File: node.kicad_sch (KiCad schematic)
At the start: 13 parts, among them J3 STLINK/V2 Clone Header, U2 STM32L151RCTx

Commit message: feat: in progress rework
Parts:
- removed D18: Node Active LED, LED_SMD:LED_0603_1608Metric, symbol Device:LED
- removed J3: STLINK/V2 Clone Header, Connector_PinHeader_2.54mm:PinHeader_2x05_P2.54mm_Vertical, symbol Connector_Generic:Conn_02x05_Odd_Even
- removed R19: 5.1K, Resistor_SMD:R_0603_1608Metric, symbol Device:R
- added J3: USB-C, Connector_USB:USB_C_Receptacle_G-Switch_GT-USB-7010ASV, symbol Connector:USB_C_Receptacle_USB2.0_14P
- added J4: UART, symbol Connector_Generic:Conn_01x04
- added J8: TC2030, Connector:Tag-Connect_TC2030-IDC-FP_2x03_P1.27mm_Vertical, symbol Connector:Conn_ARM_SWD_TagConnect_TC2030
- added R16, R17: 5.1K, symbol Device:R
- added U3: USBLC6-2SC6, Package_TO_SOT_SMD:SOT-23-6, symbol Power_Protection:USBLC6-2SC6
- added Y1: 16MHz, symbol Device:Crystal_GND24
- R14: footprint Resistor_SMD:R_0603_1608Metric -> (none)
- U2: value STM32L151RCTx -> STM32L151RCT6
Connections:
- net +3V3: now also J4.1 (Pin_1), J8.1 (VCC)
- net CS_1: now also U2.33 (PB12); no longer U2.20 (PA4)
- net CS_10: now also U2.16 (PA2); no longer U2.4 (PC15)
- net CS_11: now also U2.15 (PA1); no longer U2.3 (PC14)
- net CS_12: now also U2.14 (PA0); no longer U2.2 (PC13)
- net CS_2: now also U2.30 (PB11); no longer U2.17 (PA3)
- net CS_3: now also U2.29 (PB10); no longer U2.16 (PA2)
- net CS_4: now also U2.27 (PB1); no longer U2.15 (PA1)
- net CS_5: now also U2.26 (PB0); no longer U2.14 (PA0)
- net CS_6: now also U2.25 (PC5); no longer U2.11 (PC3)
- net CS_7: now also U2.24 (PC4); no longer U2.10 (PC2)
- net CS_8: now also U2.20 (PA4); no longer U2.9 (PC1)
- net CS_9: now also U2.17 (PA3); no longer U2.8 (PC0)
- net GND: now also R14.2, J3.A1 (GND), J3.A12 (GND), J3.B1 (GND), J3.B12 (GND), J3.S1 (SHIELD), J4.4 (Pin_4), J8.5 (GND), R16.2, R17.2, U3.2 (GND), Y1.2, Y1.4; no longer R14.1
- net P_MISO: now also U2.35 (PB14); no longer U2.22 (PA6)
- net P_MOSI: now also U2.36 (PB15); no longer U2.23 (PA7)
- net P_SCLK: now also U2.34 (PB13); no longer U2.21 (PA5)
- net RESET: now also J8.3 (~{RESET})
- net R_CS: now also U2.11 (PC3); no longer U2.54 (PD2)
- net S_MISO: now also U2.22 (PA6); no longer U2.35 (PB14)
- net S_MOSI: now also U2.23 (PA7); no longer U2.36 (PB15)
- net S_SCLK: now also U2.21 (PA5); no longer U2.34 (PB13)
- net BOOT0: now reaches U2.60 (BOOT0)
- net BOOT0: now also R14.1; no longer R14.2
- net USB_D-: now reaches U2.44 (PA11)
- net USB_D-: now also U3.6 (I/O1)
- net USB_D+: now reaches U2.45 (PA12)
- net USB_D+: now also U3.4 (I/O2)
- net HSE+: now reaches U2.5 (PH0)
- net HSE+: now also Y1.1
- net HSE-: now reaches U2.6 (PH1)
- net HSE-: now also Y1.3
- net JTDO: no longer names the net of U2.55 (PB3)
- net NJTRST: no longer names the net of U2.56 (PB4)
- net SWCLK renamed SWD_CLK
- net SWD_CLK: now also J8.4 (SWCLK)
- net SWDIO renamed SWD_IO
- net SWD_IO: now also J8.2 (SWDIO)
- net USART_RX renamed UART_RX
- net UART_RX: now also J4.2 (Pin_2)
- net USART_TX renamed UART_TX
- net UART_TX: now also J4.3 (Pin_3)
- new net: J3.A4 (VBUS), J3.A9 (VBUS), J3.B4 (VBUS), J3.B9 (VBUS), U3.5 (VBUS)
- new net: J3.A5 (CC1), R16.1
- new net: J3.B5 (CC2), R17.1
- new net USB_DT+: J3.A6 (D+), J3.B6 (D+), U3.3 (I/O2)
- new net USB_DT-: J3.A7 (D-), J3.B7 (D-), U3.1 (I/O1)
- no-connect marks 22 -> 19
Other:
- note added: "- Ability to Self Power-Cycle"
- note added: "- External Watchdog"
- note added: "3V3 UART"
- note added: "Things to be added:"
- moved on the sheet: C10, C4, C5, C6, C7, C8, C9, TP11, U2

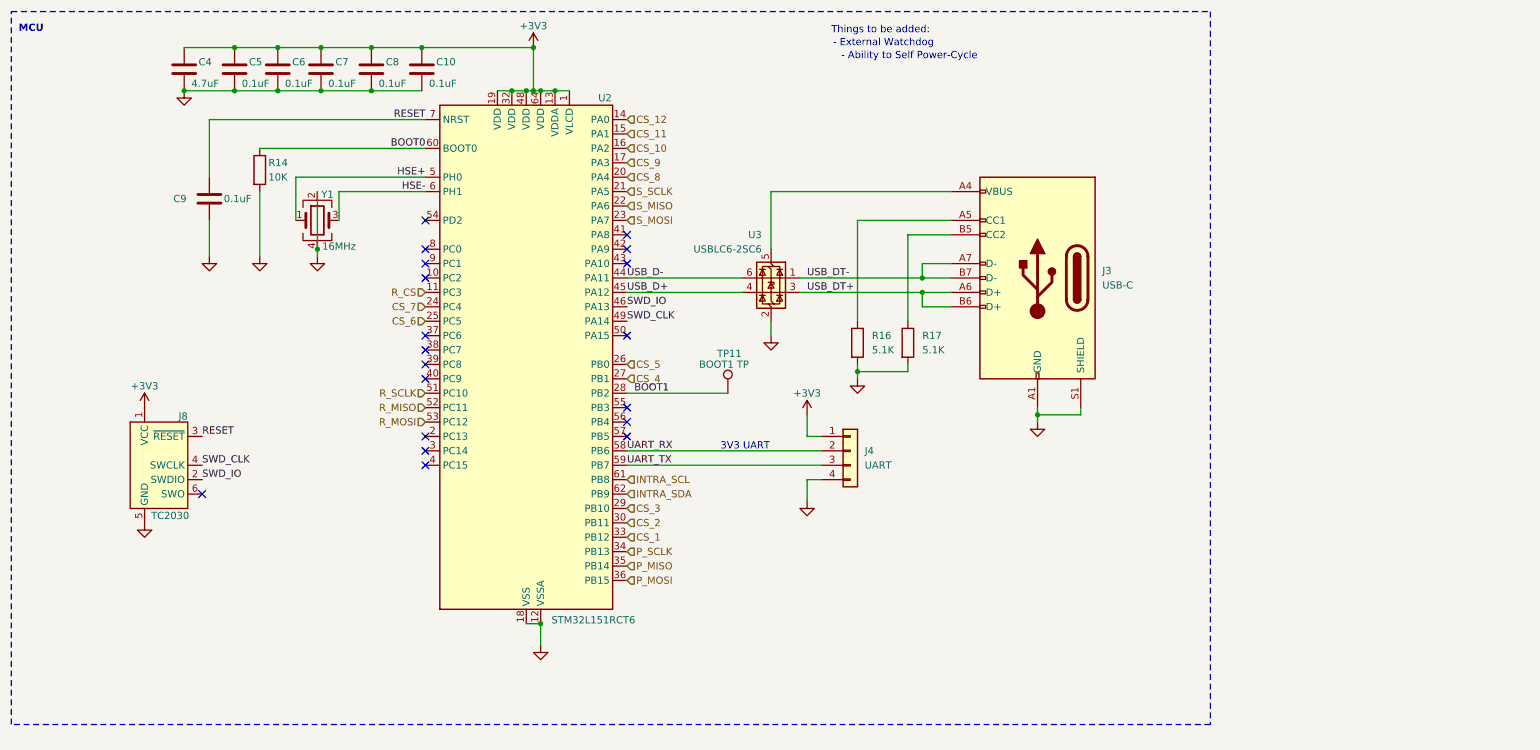
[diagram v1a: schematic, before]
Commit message: feat: trying out a diff mcu
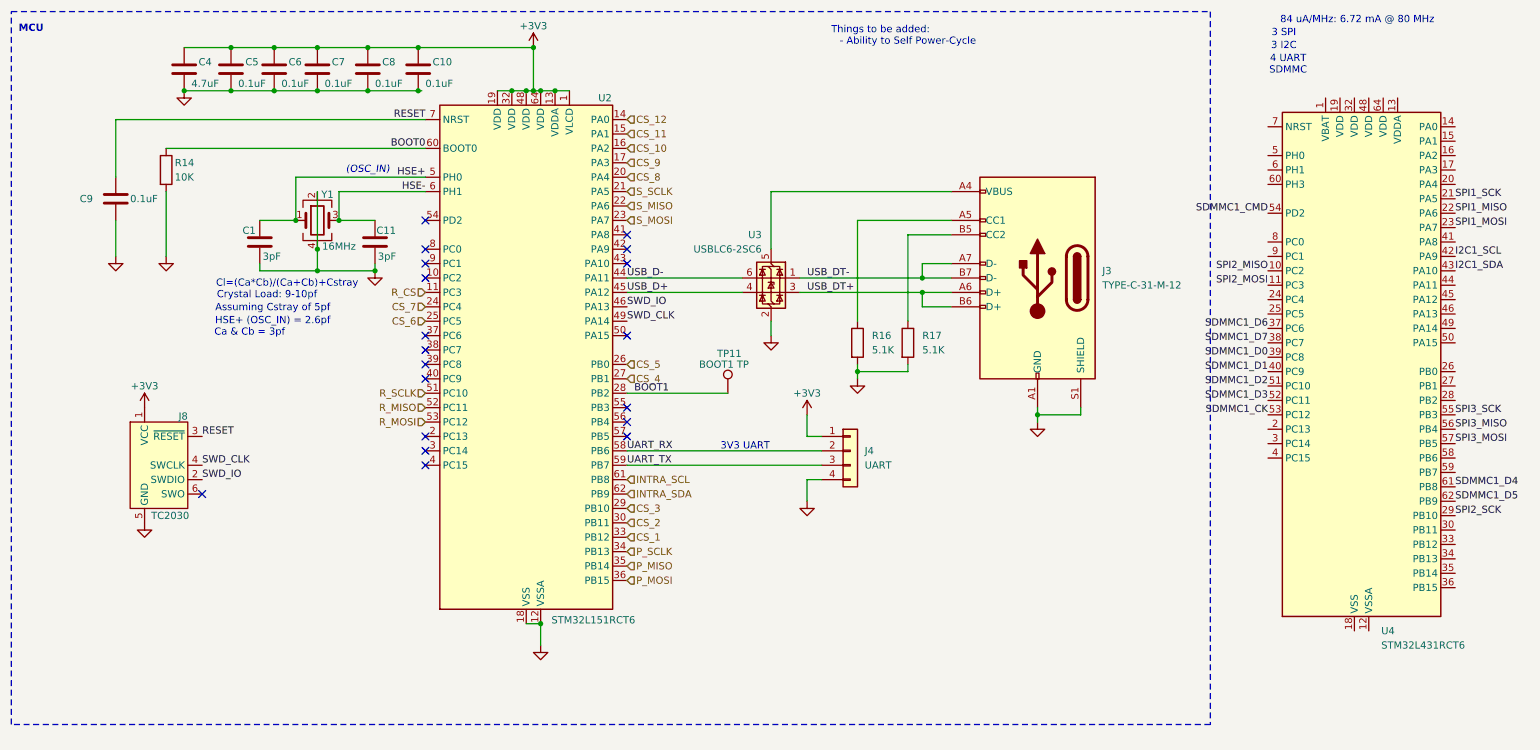
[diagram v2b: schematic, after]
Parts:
- added C1, C11: 3pF, Capacitor_SMD:C_0603_1608Metric, symbol Device:C
- added U4: STM32L431RCT6, Package_QFP:LQFP-64_10x10mm_P0.5mm, symbol MCU_ST_STM32L4:STM32L431RCTx
- J3: value USB-C -> TYPE-C-31-M-12; JLCPCB (none) -> TYPE-C-31-M-12; LCSC (none) -> C165948
- U2: LCSC (none) -> C124721
- U3: JLCPCB (none) -> USBLC6-2SC6; LCSC (none) -> C2827654
- Y1: footprint (none) -> Crystal:Crystal_SMD_3225-4Pin_3.2x2.5mm; JLCPCB (none) -> X322516MLB4SI; LCSC (none) -> C13738
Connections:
- net GND: now also C1.2, C11.2
- net HSE+: now also C1.1
- net HSE-: now also C11.1
- new net: U4.18 (VSS), U4.31 (VSS), U4.47 (VSS), U4.63 (VSS)
- new net I2C1_SCL: U4.42 (PA9)
- new net I2C1_SDA: U4.43 (PA10)
- new net SDMMC1_CK: U4.53 (PC12)
- new net SDMMC1_CMD: U4.54 (PD2)
- new net SDMMC1_D0: U4.39 (PC8)
- new net SDMMC1_D1: U4.40 (PC9)
- new net SDMMC1_D2: U4.51 (PC10)
- new net SDMMC1_D3: U4.52 (PC11)
- new net SDMMC1_D4: U4.61 (PB8)
- new net SDMMC1_D5: U4.62 (PB9)
- new net SDMMC1_D6: U4.37 (PC6)
- new net SDMMC1_D7: U4.38 (PC7)
- new net SPI1_MISO: U4.22 (PA6)
- new net SPI1_MOSI: U4.23 (PA7)
- new net SPI1_SCK: U4.21 (PA5)
- new net SPI2_MISO: U4.10 (PC2)
- new net SPI2_MOSI: U4.11 (PC3)
- new net SPI2_SCK: U4.29 (PB10)
- new net SPI3_MISO: U4.56 (PB4)
- new net SPI3_MOSI: U4.57 (PB5)
- new net SPI3_SCK: U4.55 (PB3)
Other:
- note added: "(OSC_IN)"
- note added: "3 I2C"
- note added: "3 SPI"
- note added: "4 UART"
- note added: "84 uA/MHz: 6.72 mA @ 80 MHz"
- note added: "Assuming Cstray of 5pf"
- note added: "Ca & Cb = 3pf"
- note added: "Cl=(Ca*Cb)/(Ca+Cb)+Cstray"
- note added: "Crystal Load: 9-10pf"
- note added: "HSE+ (OSC_IN) = 2.6pf"
- note added: "SDMMC"
- note removed: "- External Watchdog"
- moved on the sheet: C10, C5, C6, C7, C8, C9, R14

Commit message: Rearrange certain components
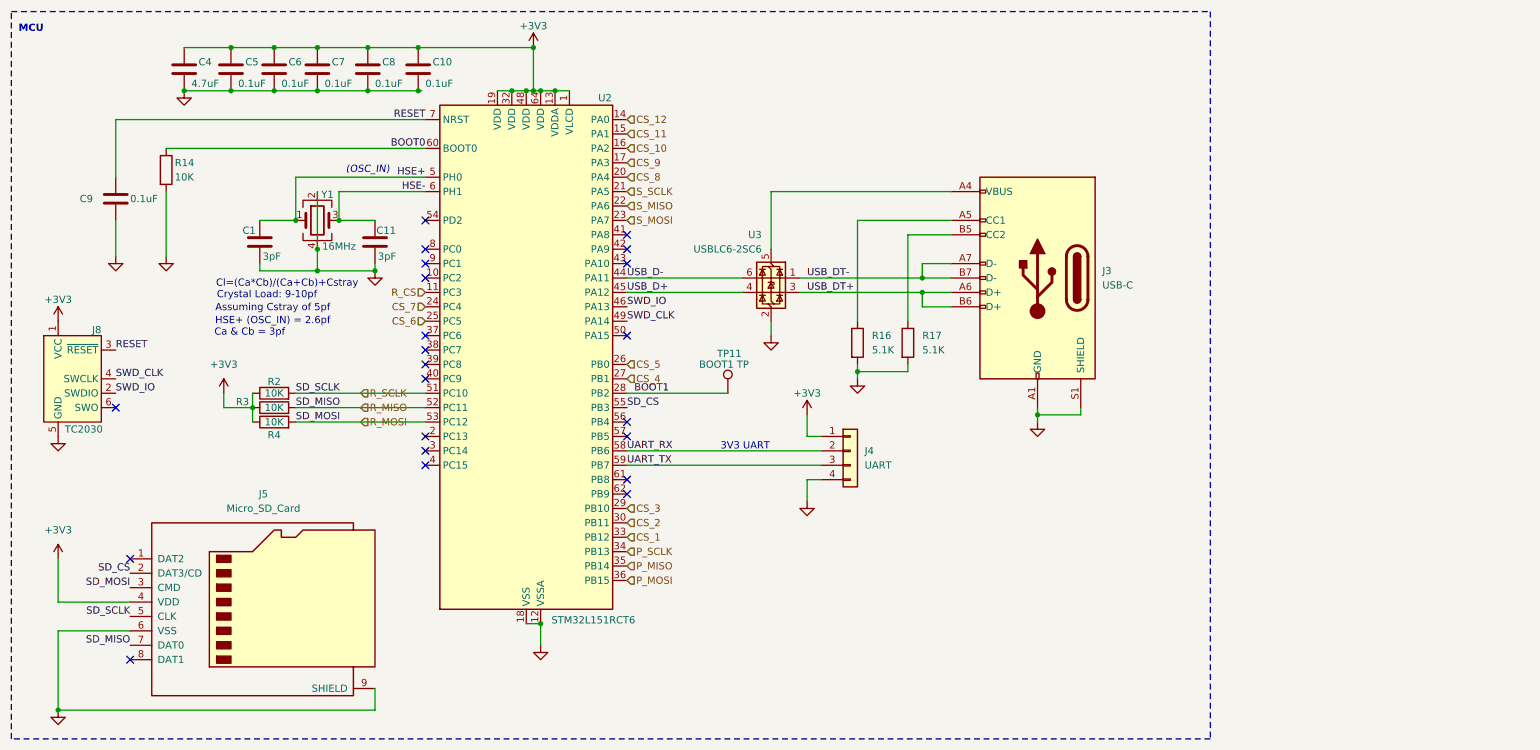
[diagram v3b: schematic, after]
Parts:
- removed U4: STM32L431RCT6, Package_QFP:LQFP-64_10x10mm_P0.5mm, symbol MCU_ST_STM32L4:STM32L431RCTx
- added J5: Micro_SD_Card, symbol Connector:Micro_SD_Card
- added R2, R3, R4: 10K, symbol Device:R
- J3: value TYPE-C-31-M-12 -> USB-C
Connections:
- net +3V3: now also J5.4 (VDD), R2.1, R3.1, R4.1
- net GND: now also J5.6 (VSS), J5.9 (SHIELD)
- net R_MISO: now also J5.7 (DAT0), R3.2
- net R_MOSI: now also J5.3 (CMD), R4.2
- net R_SCLK: now also J5.5 (CLK), R2.2
- net SD_CS: now reaches U2.55 (PB3)
- net SD_CS: now also J5.2 (DAT3/CD)
- net INTRA_SCL: no longer names the net of U2.61 (PB8)
- net INTRA_SDA: no longer names the net of U2.62 (PB9)
- no-connect marks 19 -> 22
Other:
- note removed: "- Ability to Self Power-Cycle"
- note removed: "3 I2C"
- note removed: "3 SPI"
- note removed: "4 UART"
- note removed: "84 uA/MHz: 6.72 mA @ 80 MHz"
- note removed: "SDMMC"
- note removed: "Things to be added:"
- moved on the sheet: J8

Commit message: switch to STM32L431
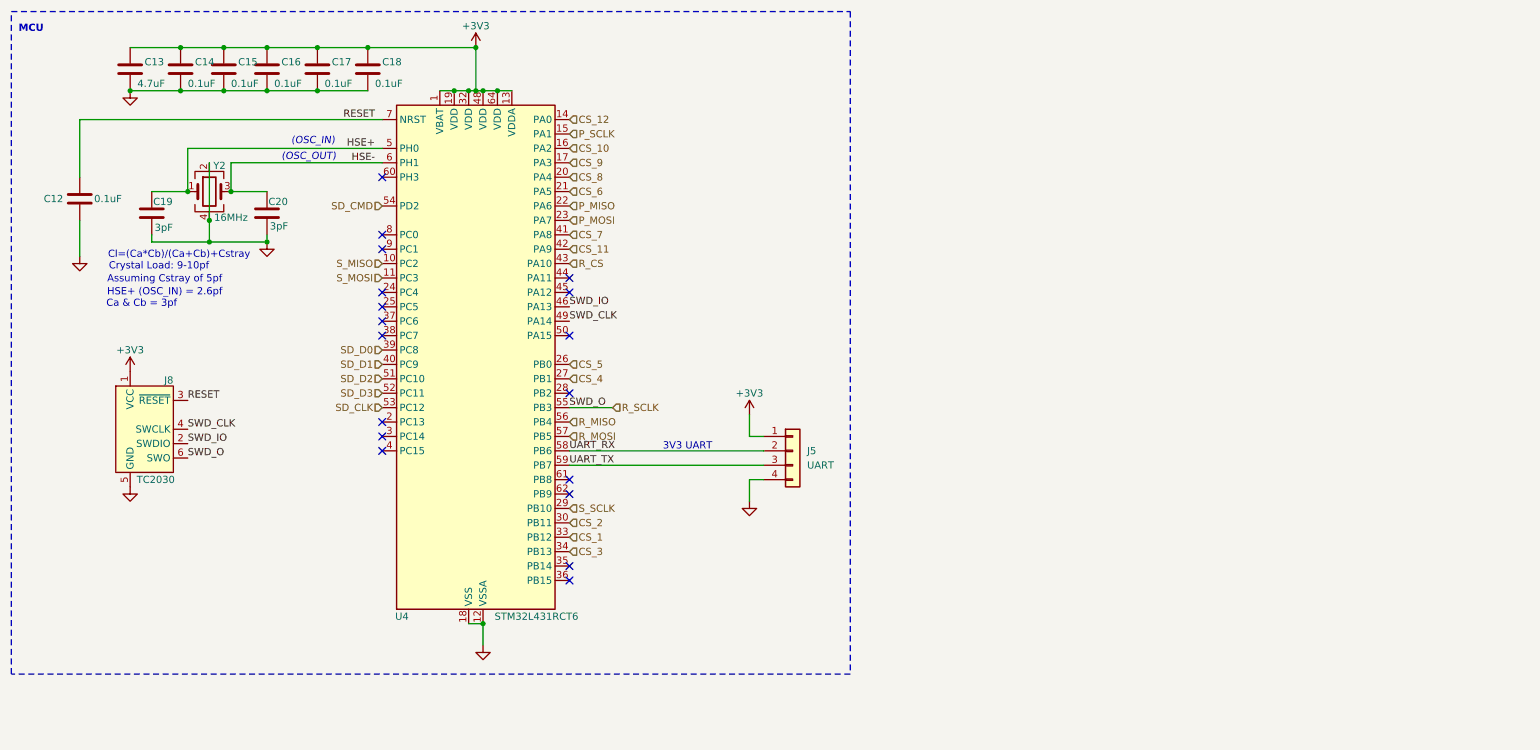
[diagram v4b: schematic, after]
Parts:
- removed C1, C11: 3pF, Capacitor_SMD:C_0603_1608Metric, symbol Device:C
- removed C10, C5, C6, C7, C8, C9: 0.1uF, Capacitor_SMD:C_0603_1608Metric, symbol Device:C
- removed C4: 4.7uF, Capacitor_SMD:C_0603_1608Metric, symbol Device:C
- removed J3: USB-C, Connector_USB:USB_C_Receptacle_G-Switch_GT-USB-7010ASV, symbol Connector:USB_C_Receptacle_USB2.0_14P
- removed J4: UART, symbol Connector_Generic:Conn_01x04
- removed J5: Micro_SD_Card, symbol Connector:Micro_SD_Card
- removed R14, R2, R3, R4: 10K, symbol Device:R
- removed R16, R17: 5.1K, symbol Device:R
- removed TP11: BOOT1 TP, TestPoint:TestPoint_Pad_D1.0mm, symbol Connector:TestPoint
- removed U2: STM32L151RCT6, Package_QFP:LQFP-64_10x10mm_P0.5mm, symbol MCU_ST_STM32L1:STM32L151RCTx
- removed U3: USBLC6-2SC6, Package_TO_SOT_SMD:SOT-23-6, symbol Power_Protection:USBLC6-2SC6
- removed Y1: 16MHz, Crystal:Crystal_SMD_3225-4Pin_3.2x2.5mm, symbol Device:Crystal_GND24
- added C12, C14, C15, C16, C17, C18: 0.1uF, Capacitor_SMD:C_0603_1608Metric, symbol Device:C
- added C13: 4.7uF, Capacitor_SMD:C_0603_1608Metric, symbol Device:C
- added C19, C20: 3pF, Capacitor_SMD:C_0603_1608Metric, symbol Device:C
- added J5: UART, symbol Connector_Generic:Conn_01x04
- added U4: STM32L431RCT6, Package_QFP:LQFP-64_10x10mm_P0.5mm, symbol MCU_ST_STM32L4:STM32L431RCTx
- added Y2: 16MHz, Crystal:Crystal_SMD_3225-4Pin_3.2x2.5mm, symbol Device:Crystal_GND24
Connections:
- net +3V3: now also C13.1, C14.1, C15.1, C16.1, C17.1, C18.1, J5.1 (Pin_1), U4.1 (VBAT), U4.13 (VDDA), U4.19 (VDD), U4.32 (VDD), U4.48 (VDD), U4.64 (VDD)
- net CS_1: now also U4.33 (PB12)
- net CS_10: now also U4.16 (PA2)
- net CS_11: now also U4.42 (PA9)
- net CS_12: now also U4.14 (PA0)
- net CS_2: now also U4.30 (PB11)
- net CS_3: now also U4.34 (PB13)
- net CS_4: now also U4.27 (PB1)
- net CS_5: now also U4.26 (PB0)
- net CS_6: now also U4.21 (PA5)
- net CS_7: now also U4.41 (PA8)
- net CS_8: now also U4.20 (PA4)
- net CS_9: now also U4.17 (PA3)
- net GND: now also C12.2, C13.2, C14.2, C15.2, C16.2, C17.2, C18.2, C19.2, C20.2, J5.4 (Pin_4), U4.12 (VSSA), U4.18 (VSS), U4.31 (VSS), U4.47 (VSS), U4.63 (VSS), Y2.2, Y2.4
- net HSE+: now also C19.1, U4.5 (PH0), Y2.1
- net HSE-: now also C20.1, U4.6 (PH1), Y2.3
- net P_MISO: now also U4.22 (PA6)
- net P_MOSI: now also U4.23 (PA7)
- net P_SCLK: now also U4.15 (PA1)
- net RESET: now also C12.1, U4.7 (NRST)
- net R_CS: now also U4.43 (PA10)
- net R_MISO: now also U4.56 (PB4)
- net R_MOSI: now also U4.57 (PB5)
- net R_SCLK: now also J8.6 (SWO), U4.55 (PB3)
- net SWD_CLK: now also U4.49 (PA14)
- net SWD_IO: now also U4.46 (PA13)
- net S_MISO: now also U4.10 (PC2)
- net S_MOSI: now also U4.11 (PC3)
- net S_SCLK: now also U4.29 (PB10)
- net UART_RX: now also J5.2 (Pin_2), U4.58 (PB6)
- net UART_TX: now also J5.3 (Pin_3), U4.59 (PB7)
- new net SD_CLK: U4.53 (PC12)
- new net SD_CMD: U4.54 (PD2)
- new net SD_D0: U4.39 (PC8)
- new net SD_D1: U4.40 (PC9)
- new net SD_D2: U4.51 (PC10)
- new net SD_D3: U4.52 (PC11)
- no-connect marks 22 -> 18
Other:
- note added: "(OSC_OUT)"
- moved on the sheet: J8
